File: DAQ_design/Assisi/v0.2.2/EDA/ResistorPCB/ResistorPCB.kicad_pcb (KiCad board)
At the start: 2 copper layers, 52.1 x 104.8 mm, 12 parts, among them J1 7-POS Plug Terminal, J2 Two-Probe Measurement, J3 7-POS Plug Terminal, J4 Four-Probe Measurement

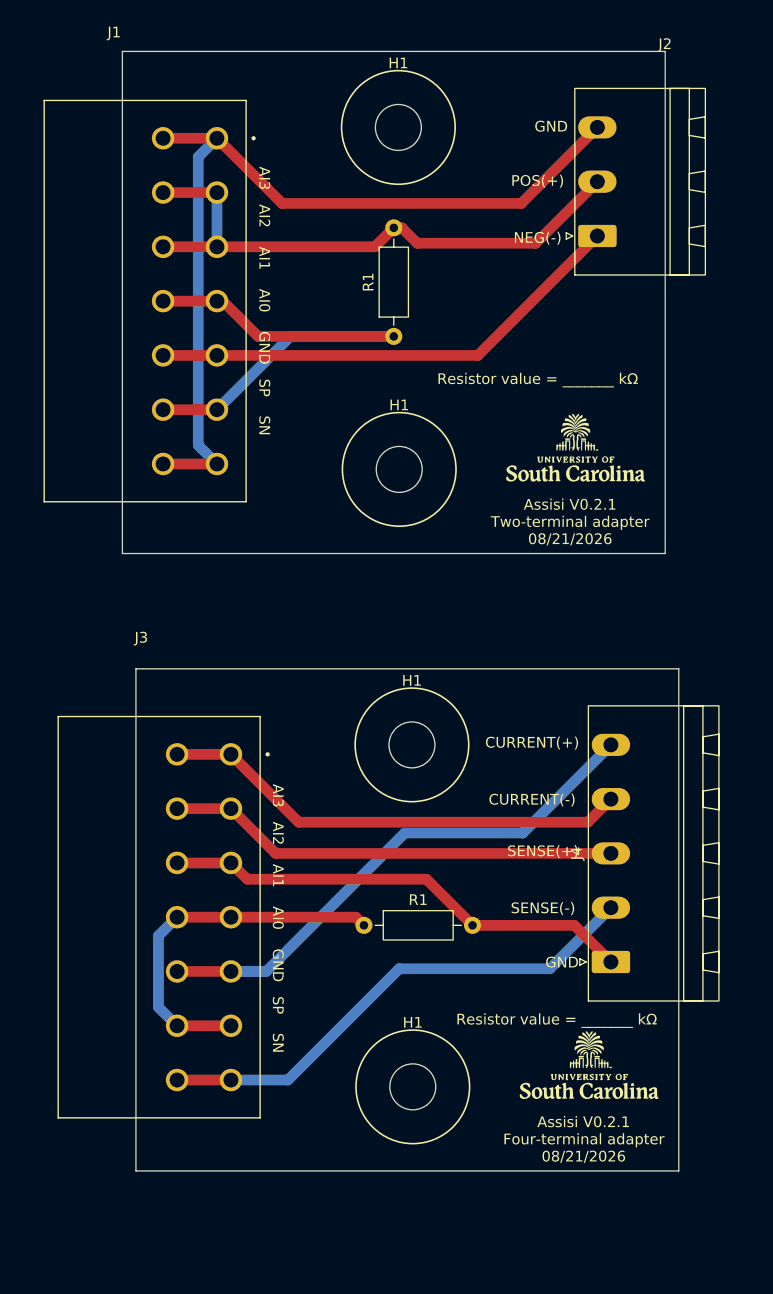
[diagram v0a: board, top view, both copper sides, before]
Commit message: Updates: GND moved, one mounting hole, resistor label moved
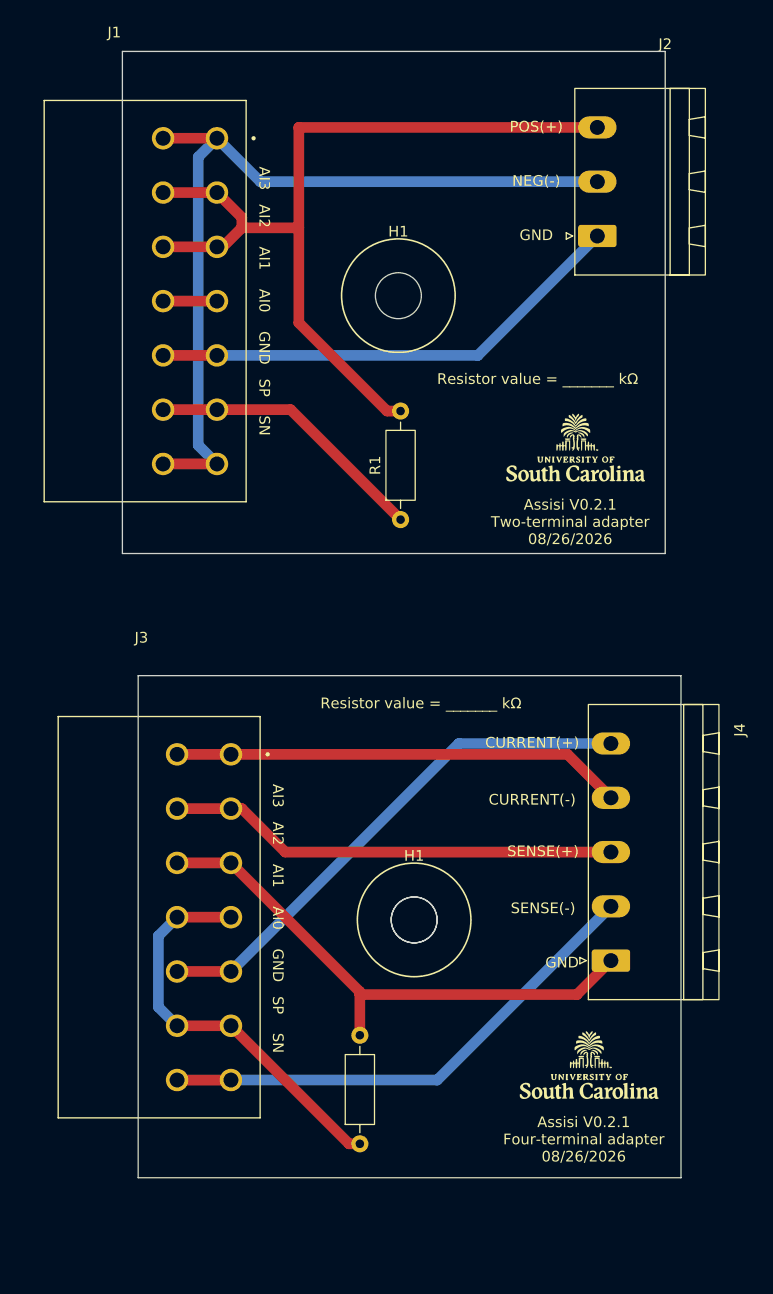
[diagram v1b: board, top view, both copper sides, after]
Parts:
- removed the H1 at (159.3, 68.3)
- removed the H1 at (160.4, 94.1)
- removed the H1 at (160.5, 126.1)
- added ?: , , F.Cu at (160.7, 110.5)
- added H1: MountingHole_Pad, MountingHole:MountingHole_4.3mm_M4, F.Cu at (160.7, 110.5)
- moved R2 20.5 mm to (155.6, 131.4), turned to 90 degrees
- moved R1 17.2 mm to (159.4, 73.0)
- moved H1 15.7 mm to (159.2, 52.1)
- moved J4 0.13 mm to (179.1, 114.3)
- renumbered R1 to R2
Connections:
- J2 pad 2: Net-(J1-1) -> Net-(J1-3)
- J2 pad 3: Net-(J1-3) -> Net-(J1-1)
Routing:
- net Net-(J1-1): track 54.5 -> 81.9 mm
- net Net-(J1-0): track 47.4 -> 31.5 mm
- net Net-(J3-1): track 44.4 -> 51.7 mm
- net Net-(J3-0): track 34.5 -> 38.3 mm
- net Net-(J1-3): track 83.1 -> 79.3 mm
- net Net-(J3-3): track 44.1 -> 42.3 mm
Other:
- board size 52.1 x 104.8 mm -> 52.3 x 105.4 mm
- board text added: "Assisi V0.2.1 Four-terminal adapter 08/26/2026"
- board text added: "Assisi V0.2.1 Two-terminal adapter 08/26/2026"
- board text removed: "${REFERENCE}"
- board text removed: "Assisi V0.2.1 Four-terminal adapter 08/21/2026"
- board text removed: "Assisi V0.2.1 Two-terminal adapter 08/21/2026"

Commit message: Separated PCBs: Two-Probe and Four-Probe
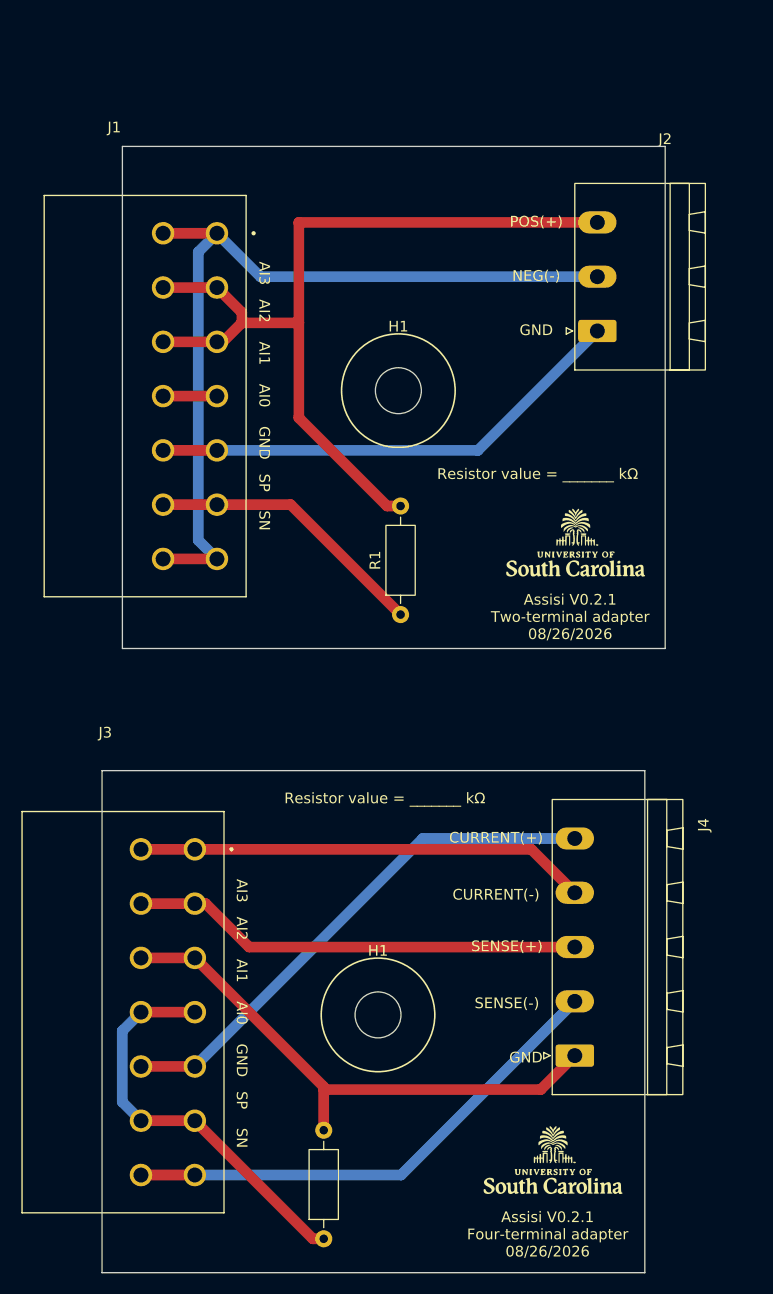
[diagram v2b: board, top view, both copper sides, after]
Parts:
- removed ?: , 
- moved R2 9.51 mm to (152.2, 140.3)
- moved G2 9.51 mm to (173.7, 133.0)
- moved H1 9.51 mm to (157.3, 119.4)
- moved J3 9.51 mm to (124.0, 100.3)
- moved J4 9.51 mm to (175.7, 123.2)
- moved G2 8.89 mm to (175.8, 75.2)
- moved H1 8.89 mm to (159.2, 61.0)
- moved J1 8.89 mm to (126.0, 42.7)
- moved J2 8.89 mm to (177.8, 55.4)
- moved R1 8.89 mm to (159.4, 81.9)
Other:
- board size 52.3 x 105.4 mm -> 52.7 x 105.4 mm
